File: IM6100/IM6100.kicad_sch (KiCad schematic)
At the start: 0 parts

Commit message: PCB for IM6100, PDP-8 ISA compatible 12 bit microprocessor.
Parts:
- added C1, C2: 22pF, Capacitor_THT:C_Disc_D3.8mm_W2.6mm_P2.50mm, symbol Device:C
- added C10, C11, C3, C4, C5, C6, C7, C8, C9: 0.1uF, 0my_project:C_1608_0603, symbol Device:C
- added C18: 1uF, 0my_project:C_1608_0603, symbol Device:C
- added IMG1: Logo_image, 0my_project:Icon_Nosuz, symbol 0my_project:Logo_image
- added R1: 1M, Resistor_THT:R_Axial_DIN0207_L6.3mm_D2.5mm_P10.16mm_Horizontal, symbol Device:R
- added R2: 51K, 0my_project:R_1608_0603, symbol Device:R
- added U1: IM6100, 0my_project:DIP-40_IM6100, symbol 0my_project:IM6100
- added U2, U3, U4, U5: TXB0108PW, Package_SO:TSSOP-20_4.4x6.5mm_P0.65mm, symbol Logic_LevelTranslator:TXB0108PW
- added U6: Tang_Nano_9K, 0my_project:DIP-48_TangNano9K, symbol 0my_project:Tang_Nano_9K
- added Y1: 4MHz, 0my_project:Y_2P, symbol Device:Crystal
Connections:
- new net: C2.2, R1.2, U1.15 (OSC_IN), Y1.1
- new net: C1.2, R1.1, U1.14 (OSC_OUT), Y1.2
- new net +3.3V: C10.1, C4.1, C6.1, C8.1, U2.10 (OE), U2.2 (V_{CCA}), U3.10 (OE), U3.2 (V_{CCA}), U4.10 (OE), U4.2 (V_{CCA}), U5.10 (OE), U5.2 (V_{CCA}), U6.25 (3V3)
- new net +5V: C11.1, C18.1, C3.1, C5.1, C7.1, C9.1, U1.1 (Vcc), U1.11 (~{WAIT}), U1.8 (~{INTREQ}), U2.19 (V_{CCB}), U3.19 (V_{CCB}), U4.19 (V_{CCB}), U5.19 (V_{CCB}), U6.31 (5V)
- new net CLEAR_SW: U6.41 (80_IOT12A_1V8)
- new net CONT_SW: U6.47 (86_IOT8A_1V8)
- new net CPREQ_ON: U6.39 (77_IOT37A)
- new net DEP_SW: U6.48 (63_IOR5A)
- new net DISP_CLK: U6.28 (31_IOB15A)
- new net DMAGNT: U1.3 (DMAGNT), U2.18 (B2)
- new net DMAGNT_3V3: U2.3 (A2), U6.32 (70_IOT41B)
- new net DX0: U1.16 (DX0), U3.20 (B1)
- new net DX0_3V3: U3.1 (A1), U6.5 (25_IOB8A)
- new net DX1: U1.17 (DX1), U3.18 (B2)
- new net DX10: U1.27 (DX10), U5.14 (B6)
- new net DX10_3V3: U5.7 (A6), U6.19 (54_IOR15A)
- new net DX11: U1.28 (DX11), U5.13 (B7)
- new net DX11_3V3: U5.8 (A7), U6.18 (53_IOR15B)
- new net DX1_3V3: U3.3 (A2), U6.6 (26_IOB8B)
- new net DX2: U1.18 (DX2), U3.17 (B3)
- new net DX2_3V3: U3.4 (A3), U6.7 (27_IOB11A)
- new net DX3: U1.19 (DX3), U3.16 (B4)
- new net DX3_3V3: U3.5 (A4), U6.8 (28_IOB11B)
- new net DX4: U1.20 (DX4), U3.15 (B5)
- new net DX4_3V3: U3.6 (A5), U6.9 (29_IOB13A)
- new net DX5: U1.21 (DX5), U5.20 (B1)
- new net DX5_3V3: U5.1 (A1), U6.24 (69_IOT42A)
- new net DX6: U1.22 (DX6), U5.18 (B2)
- new net DX6_3V3: U5.3 (A2), U6.23 (68_IOT42B)
- new net DX7: U1.23 (DX7), U5.17 (B3)
- new net DX7_3V3: U5.4 (A3), U6.22 (57_IOR13A)
- new net DX8: U1.24 (DX8), U5.16 (B4)
- new net DX8_3V3: U5.5 (A4), U6.21 (56_IOR14A)
- new net DX9: U1.25 (DX9), U5.15 (B5)
- new net DX9_3V3: U5.6 (A5), U6.20 (55_IOR14B)
- new net EXAM_SW: U6.43 (82_IOT11A_1V8)
- new net GND: C1.1, C10.2, C11.2, C18.2, C2.1, C3.2, C4.2, C5.2, C6.2, C7.2, C8.2, C9.2, R2.2, U1.26 (GND), U2.11 (GND), U3.11 (GND), U3.12 (B8), U3.13 (B7), U3.14 (B6), U3.7 (A6), U3.8 (A7), U3.9 (A8), U4.11 (GND), U5.11 (GND), U6.26 (GND)
- new net LD_ADDR_SW: U6.42 (81_IOT11B_1V8)
- new net LINK: U1.29 (LINK), U5.12 (B8)
- new net LINK_3V3: U5.9 (A8)
- new net LXMAR: U1.10 (LXMAR), U2.12 (B8)
- new net LXMAR_3V3: U2.9 (A8), U6.38 (76_IOT37B)
- new net MODE_SW0: U6.46 (85_IOT8B_1V8)
- new net MODE_SW1: U6.45 (84_IOT10A_1V8)
- new net MODE_SW2: U6.44 (83_IOT10B_1V8)
- new net PC_CLK: U6.29 (49_IOR24A)
- new net RUN: U1.2 (RUN), U2.20 (B1)
- new net RUN_3V3: U2.1 (A1), U6.30 (48_IOR24B)
- new net SINGLE_SW: U6.40 (79_IOT12B_1V8)
- new net XTA: U1.9 (XTA), U2.13 (B7)
- new net XTA_3V3: U2.8 (A7), U6.37 (75_IOT38A)
- new net ~{C0_3V3}: U4.4 (A3), U6.15 (41_IOB41A)
- new net ~{C0}: U1.32 (~{C0}), U4.17 (B3)
- new net ~{C1_3V3}: U4.5 (A4), U6.14 (35_IOB29A)
- new net ~{C1}: U1.33 (~{C1}), U4.16 (B4)
- new net ~{C2_3V3}: U4.6 (A5), U6.13 (40_IOB33B)
- new net ~{C2}: U1.34 (~{C2}), U4.15 (B5)
- new net ~{CPREQ_3V3}: U2.5 (A4), U6.34 (72_IOT39B)
- new net ~{CPREQ}: U1.5 (~{CPREQ}), U2.16 (B4)
- new net ~{CPSEL_3V3}: U4.9 (A8), U6.10 (30_IOB13B)
- new net ~{CPSEL}: U1.38 (~{CPSEL}), U4.12 (B8)
- new net ~{DEVSEL_3V3}: U4.1 (A1), U6.17 (51_IOR17B)
- new net ~{DEVSEL}: U1.30 (~{DEVSEL}), U4.20 (B1)
- new net ~{DMAREQ_3V3}: U2.4 (A3), U6.33 (71_IOT41A)
- new net ~{DMAREQ}: U1.4 (~{DMAREQ}), U2.17 (B3)
- new net ~{MEMSEL_3V3}: U4.8 (A7), U6.11 (33_IOB23A)
- new net ~{MEMSEL}: U1.37 (~{MEMSEL}), U4.13 (B7)
- new net ~{RESET_3V3}: R2.1, U2.7 (A6), U6.36 (74_IOT38B)
- new net ~{RESET}: U1.7 (~{RESET}), U2.14 (B6)
- new net ~{RUN/HLT_3V3}: U2.6 (A5), U6.35 (73_IOT39A)
- new net ~{RUN/HLT}: U1.6 (~{RUN/HLT}), U2.15 (B5)
- new net ~{SKP_3V3}: U4.7 (A6), U6.12 (34_IOB23B)
- new net ~{SKP}: U1.35 (~{SKP}), U4.14 (B6)
- new net ~{SWSEL_3V3}: U4.3 (A2), U6.16 (42_IOB41B)
- new net ~{SWSEL}: U1.31 (~{SWSEL}), U4.18 (B2)
- new net ~{SW_EN}: U6.27 (32_IOB15B)
- no-connect marks 0 -> 9
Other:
- added sheet Front Panel (front-panel.kicad_sch)
- note added: "- VccA is equal or less than VccB. Max. VccA is 3.6V. Max. VccB is 5.5V. - OE is under VccA."
- note added: "XTA: Read XTB: Write"
- company: (none) -> @nosuz
- title: (none) -> PDP-8_IM6100

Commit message: Removed Pull-dow on ~RESET.
TXB0108 can't use pull-up and -down.
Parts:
- removed R2: 51K, 0my_project:R_1608_0603, symbol Device:R
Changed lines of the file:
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@@
 	)
 	(bus_entry
-		(at 144.78 30.48)
-		(size 2.54 -2.54)
-		(stroke
-			(width 0)
-			(type default)
-		)
-	)
-	(bus_entry
 		(at 181.61 73.66)
 		(size 2.54 -2.54)
@@
 	(wire
 		(pts
-			(xy 161.29 27.94) (xy 147.32 27.94)
-		)
-		(stroke
-			(width 0)
-			(type default)
-		)
-	)
-	(wire
-		(pts
 			(xy 44.45 60.96) (xy 45.72 60.96)
 		)
@@
 	(wire
 		(pts
-			(xy 161.29 27.94) (xy 161.29 29.21)
-		)
-		(stroke
-			(width 0)
-			(type default)
-		)
-	)
-	(wire
-		(pts
 			(xy 78.74 50.8) (xy 88.9 50.8)
 		)
@@
 		)
 	)
-	(wire
-		(pts
-			(xy 161.29 36.83) (xy 161.29 38.1)
-		)
-		(stroke
-			(width 0)
-			(type default)
-		)
-	)
 	(bus
 		(pts
@@
 		)
 	)
-	(label "~{RESET_3V3}"
-		(at 148.59 27.94 0)
-		(effects
-			(font
-				(size 1.27 1.27)
-			)
-			(justify left bottom)
-		)
-	)
 	(label "{IM_BUS}"
 		(at 36.83 127 0)
@@
 	)
 	(symbol
-		(lib_id "power:GND")
-		(at 161.29 38.1 0)
-		(unit 1)
-		(exclude_from_sim no)
-		(in_bom yes)
-		(on_board yes)
-		(dnp no)
-		(property "Reference" "#PWR024"
-			(at 161.29 44.45 0)
-			(effects
-				(font
-					(size 1.27 1.27)
-				)
-				(hide yes)
-			)
-		)
-		(property "Value" "GND"
-			(at 165.1 40.132 0)
-			(effects
-				(font
-					(size 1.27 1.27)
-				)
-			)
-		)
-		(property "Footprint" ""
-			(at 161.29 38.1 0)
-			(effects
-				(font
-					(size 1.27 1.27)
-				)
-				(hide yes)
-			)
-		)
-		(property "Datasheet" ""
-			(at 161.29 38.1 0)
-			(effects
-				(font
-					(size 1.27 1.27)
-				)
-				(hide yes)
-			)
-		)
-		(property "Description" "Power symbol creates a global label with name \"GND\" , ground"
-			(at 161.29 38.1 0)
-			(effects
-				(font
-					(size 1.27 1.27)
-				)
-				(hide yes)
-			)
-		)
-		(pin "1"
-		)
-		(instances
-			(project "IM6100"
-				(path "/53a0cf52-832d-4c44-bbfc-bbaea7dc652e"
-					(reference "#PWR024")
-					(unit 1)
-				)
-			)
-		)
-	)
-	(symbol
 		(lib_id "Device:R")
 		(at 38.1 50.8 0)
@@
 					(unit 1)
 				)
-			)
-		)
-	)
-	(symbol
-		(lib_id "Device:R")
-		(at 161.29 33.02 0)
-		(unit 1)
-		(exclude_from_sim no)
-		(in_bom yes)
-		(on_board yes)
-		(dnp no)
-		(property "Reference" "R2"
-			(at 163.068 30.226 0)
-			(effects
-				(font
-					(size 1.27 1.27)
-				)
-				(justify left)
-			)
-		)
-		(property "Value" "51K"
-			(at 163.068 33.02 0)
-			(effects
-				(font
-					(size 1.27 1.27)
-				)
-				(justify left)
-			)
-		)
-		(property "Footprint" "0my_project:R_1608_0603"
-			(at 159.512 33.02 90)
-			(effects
-				(font
-					(size 1.27 1.27)
-				)
-				(hide yes)
-			)
-		)
-		(property "Datasheet" "~"
-			(at 161.29 33.02 0)
-			(effects
-				(font
-					(size 1.27 1.27)
-				)
-				(hide yes)
-			)
-		)
-		(property "Description" "Resistor"
-			(at 161.29 33.02 0)
-			(effects
-				(font
-					(size 1.27 1.27)
-				)
-				(hide yes)
-			)
-		)
-		(property "LCSC" "C23196"
-			(at 161.29 33.02 0)
-			(effects
-				(font
-					(size 1.27 1.27)
-				)
-				(hide yes)
-			)
-		)
-		(pin "2"
-		)
-		(pin "1"
-		)
-		(instances
-			(project "IM6100"
-				(path "/53a0cf52-832d-4c44-bbfc-bbaea7dc652e"
-					(reference "R2")
-					(unit 1)
-				)

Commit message: Fixed to reset IM6100 during setting up Tang Nano 9K.
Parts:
- added R2: 10K, 0my_project:R_1608_0603, symbol Device:R
- added U13: SN74AHC1G04, 0my_project:SOT-23-5_TI, symbol 0my_project:SN74AHC1G04DBVR
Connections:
- net +3.3V: now also R2.2, U13.5 (Vcc)
- net GND: now also U13.3 (GND)
- net LXMAR_3V3: now also U6.37 (75_IOT38A); no longer U6.38 (76_IOT37B)
- net XTA_3V3: now also U6.36 (74_IOT38B); no longer U6.37 (75_IOT38A)
- net ~{RESET_3V3}: now also U13.4; no longer U6.36 (74_IOT38B)
- new net MK_RESET: R2.1, U13.2, U6.38 (76_IOT37B)

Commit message: Updated IC socket part number for IM6100.
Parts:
- U1: Akizuki IC socket: 100241 x 2 -> IC socket: 100034
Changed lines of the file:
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@@
 			)
 		)
-		(property "Akizuki" "IC socket: 100241 x 2"
+		(property "Akizuki" "IC socket: 100034"
 			(at 62.23 73.66 0)
 			(effects

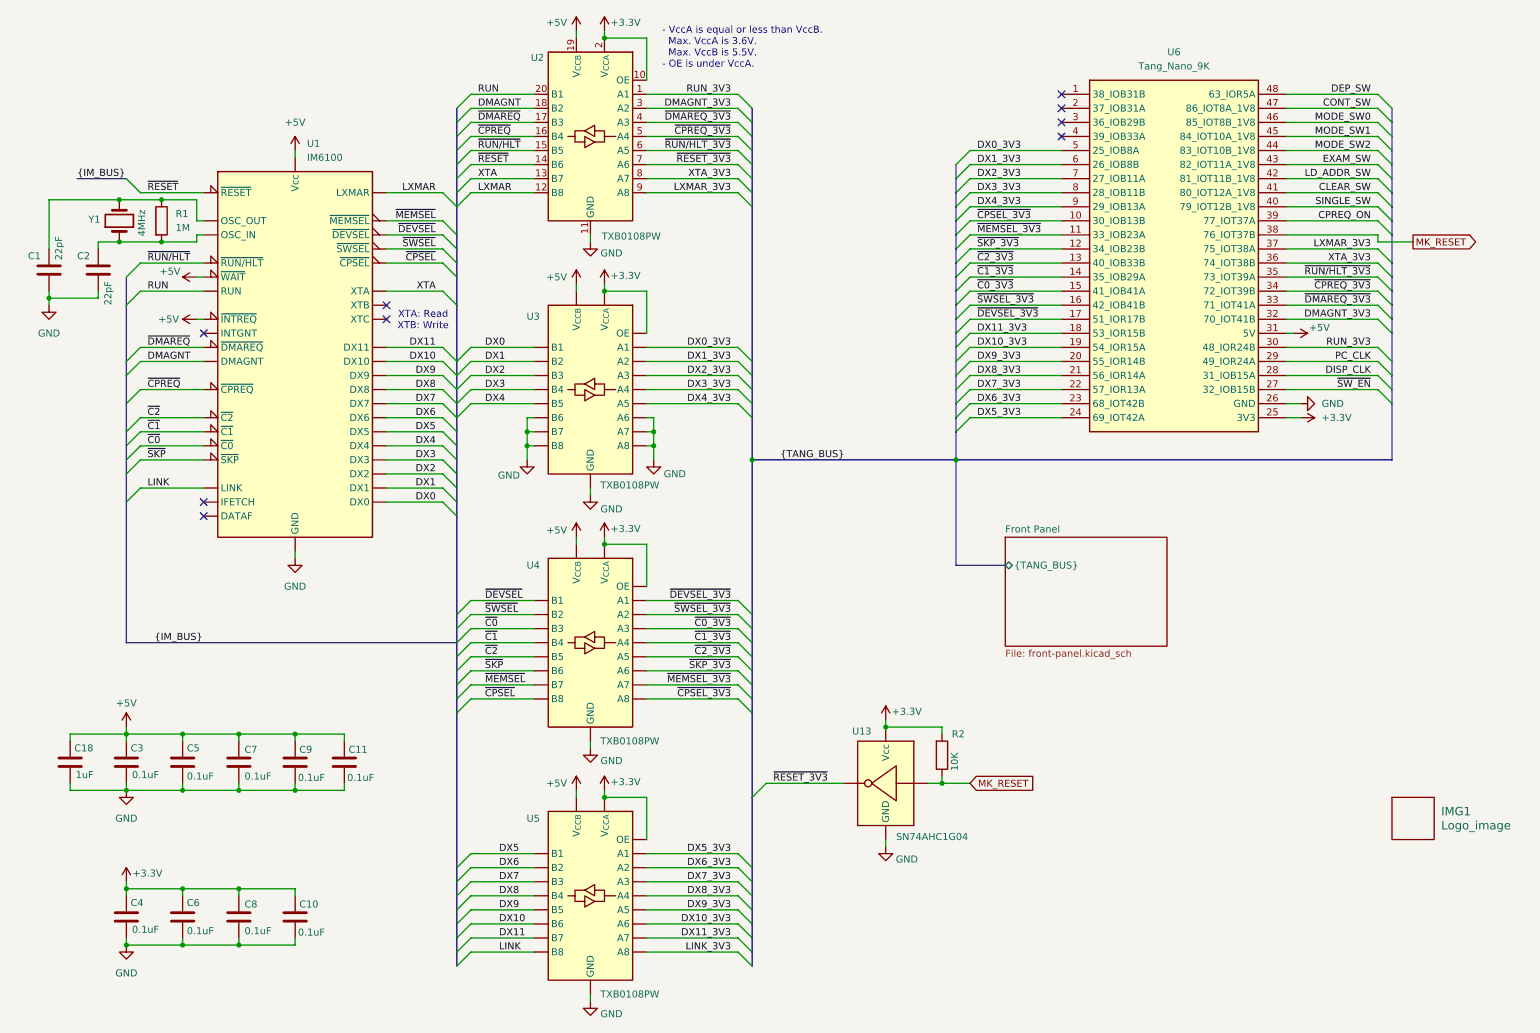
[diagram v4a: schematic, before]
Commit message: Replaced level shifter logics to SN74LVC8T245.
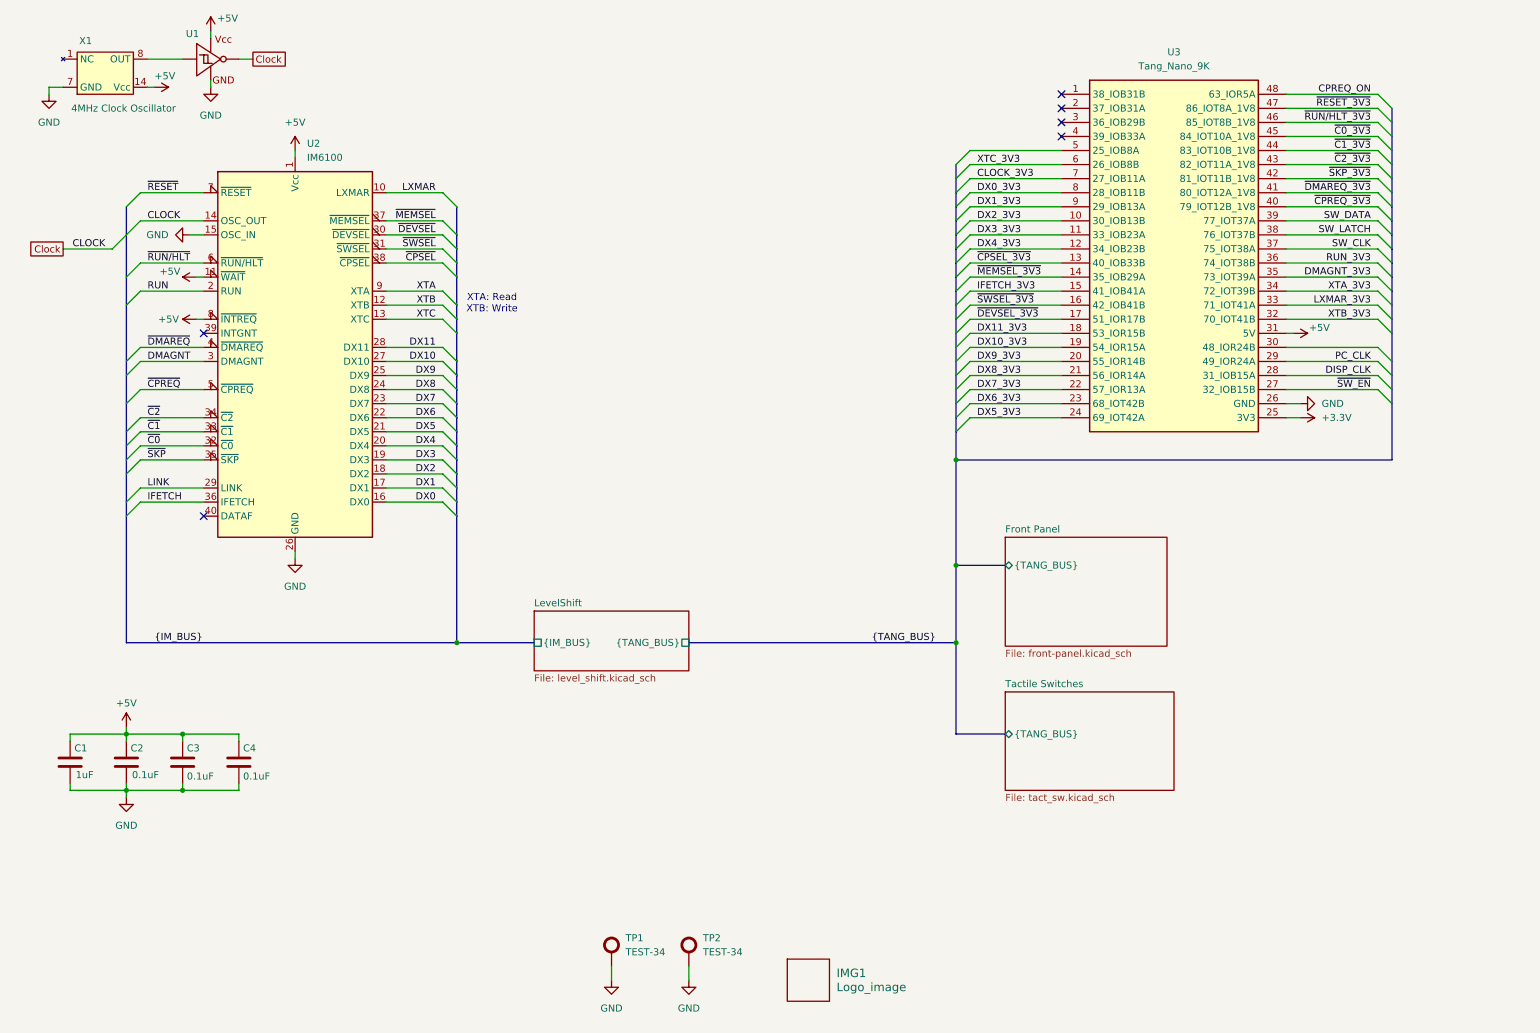
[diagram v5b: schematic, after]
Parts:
- removed C1, C2: 22pF, Capacitor_THT:C_Disc_D3.8mm_W2.6mm_P2.50mm, symbol Device:C
- removed C10, C11, C6, C7, C8, C9: 0.1uF, 0my_project:C_1608_0603, symbol Device:C
- removed R1: 1M, Resistor_THT:R_Axial_DIN0207_L6.3mm_D2.5mm_P10.16mm_Horizontal, symbol Device:R
- removed R2: 10K, 0my_project:R_1608_0603, symbol Device:R
- removed U13: SN74AHC1G04, 0my_project:SOT-23-5_TI, symbol 0my_project:SN74AHC1G04DBVR
- removed U2, U3, U4, U5: TXB0108PW, Package_SO:TSSOP-20_4.4x6.5mm_P0.65mm, symbol Logic_LevelTranslator:TXB0108PW
- removed Y1: 4MHz, 0my_project:Y_2P, symbol Device:Crystal
- added TP1, TP2: TEST-34, 0my_project:TEST-34, symbol 0my_project:TestPin
- added U1: SN74AHCT1G14DBV, 0my_project:SOT-23-5_TI, symbol 0my_project:SN74AHCT1G14DBVR
- added X1: 4MHz Clock Oscillator, 0my_project:DIP-14_ClockOscillator, symbol 0my_project:Clock_Oscillator
- renumbered C18 to C1, C3 to C2, C5 to C3, U1 to U2, U6 to U3
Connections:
- net CLEAR_SW is gone; now on net ~{DMAREQ_3V3}: U3.41 (80_IOT12A_1V8)
- net CONT_SW is gone; now on net ~{RESET_3V3}: U3.47 (86_IOT8A_1V8)
- net DEP_SW is gone; now on net CPREQ_ON: U3.48 (63_IOR5A)
- net EXAM_SW is gone; now on net ~{C2_3V3}: U3.43 (82_IOT11A_1V8)
- net LD_ADDR_SW is gone; now on net ~{SKP_3V3}: U3.42 (81_IOT11B_1V8)
- net MODE_SW0 is gone; now on net ~{RUN/HLT_3V3}: U3.46 (85_IOT8B_1V8)
- net MODE_SW1 is gone; now on net ~{C0_3V3}: U3.45 (84_IOT10A_1V8)
- net MODE_SW2 is gone; now on net ~{C1_3V3}: U3.44 (83_IOT10B_1V8)
- net SINGLE_SW is gone; now on net ~{CPREQ_3V3}: U3.40 (79_IOT12B_1V8)
- net +3.3V: no longer C4.1
- net +5V: now also C4.1, U1.5 (Vcc), X1.11 (Vcc), X1.14 (Vcc)
- net CPREQ_ON: no longer U3.39 (77_IOT37A)
- net DMAGNT_3V3: now also U3.35 (73_IOT39A); no longer U3.32 (70_IOT41B)
- net DX0_3V3: now also U3.8 (28_IOB11B); no longer U3.5 (25_IOB8A)
- net DX1_3V3: now also U3.9 (29_IOB13A); no longer U3.6 (26_IOB8B)
- net DX2_3V3: now also U3.10 (30_IOB13B); no longer U3.7 (27_IOB11A)
- net DX3_3V3: now also U3.11 (33_IOB23A); no longer U3.8 (28_IOB11B)
- net DX4_3V3: now also U3.12 (34_IOB23B); no longer U3.9 (29_IOB13A)
- net GND: now also U2.15 (OSC_IN), TP1.1 (Test), TP2.1 (Test), U1.3 (GND), X1.10 (GND), X1.12 (GND), X1.13 (GND), X1.2 (GND), X1.3 (GND), X1.5 (GND), X1.6 (GND), X1.7 (GND), X1.9 (GND)
- net LXMAR_3V3: now also U3.33 (71_IOT41A); no longer U3.37 (75_IOT38A)
- net RUN_3V3: now also U3.36 (74_IOT38B); no longer U3.30 (48_IOR24B)
- net XTA_3V3: now also U3.34 (72_IOT39B); no longer U3.36 (74_IOT38B)
- net ~{C0_3V3}: no longer U3.15 (41_IOB41A)
- net ~{C1_3V3}: no longer U3.14 (35_IOB29A)
- net ~{C2_3V3}: no longer U3.13 (40_IOB33B)
- net ~{CPREQ_3V3}: no longer U3.34 (72_IOT39B)
- net ~{CPSEL_3V3}: now also U3.13 (40_IOB33B); no longer U3.10 (30_IOB13B)
- net ~{DMAREQ_3V3}: no longer U3.33 (71_IOT41A)
- net ~{MEMSEL_3V3}: now also U3.14 (35_IOB29A); no longer U3.11 (33_IOB23A)
- net ~{RUN/HLT_3V3}: no longer U3.35 (73_IOT39A)
- net ~{SKP_3V3}: no longer U3.12 (34_IOB23B)
- net Clock: now reaches U2.14 (OSC_OUT)
- net Clock: now also U1.4 (Y)
- net XTB: now reaches U2.12 (XTB)
- net XTC: now reaches U2.13 (XTC)
- net IFETCH: now reaches U2.36 (IFETCH)
- net MK_RESET renamed SW_LATCH
- new net: U1.2 (A), X1.8 (OUT)
- new net: X1.1 (NC), X1.4 (NC)
- new net CLOCK_3V3: U3.7 (27_IOB11A)
- new net IFETCH_3V3: U3.15 (41_IOB41A)
- new net SW_CLK: U3.37 (75_IOT38A)
- new net SW_DATA: U3.39 (77_IOT37A)
- new net XTB_3V3: U3.32 (70_IOT41B)
- new net XTC_3V3: U3.6 (26_IOB8B)
- no-connect marks 9 -> 6
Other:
- added sheet LevelShift (level_shift.kicad_sch)
- added sheet Tactile Switches (tact_sw.kicad_sch)
- note removed: "- VccA is equal or less than VccB. Max. VccA is 3.6V. Max. VccB is 5.5V. - OE is under VccA."
- moved on the sheet: IMG1
